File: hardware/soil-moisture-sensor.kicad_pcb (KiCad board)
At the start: 2 copper layers, 185.3 x 23 mm, 23 parts, among them J1 AVR ISP, J2 FTDI, SW1 SW_Push, U1 ATmega328P-AU, U2 NRF24L01_Breakout, U3 ATSHA204A, Y1 Resonator

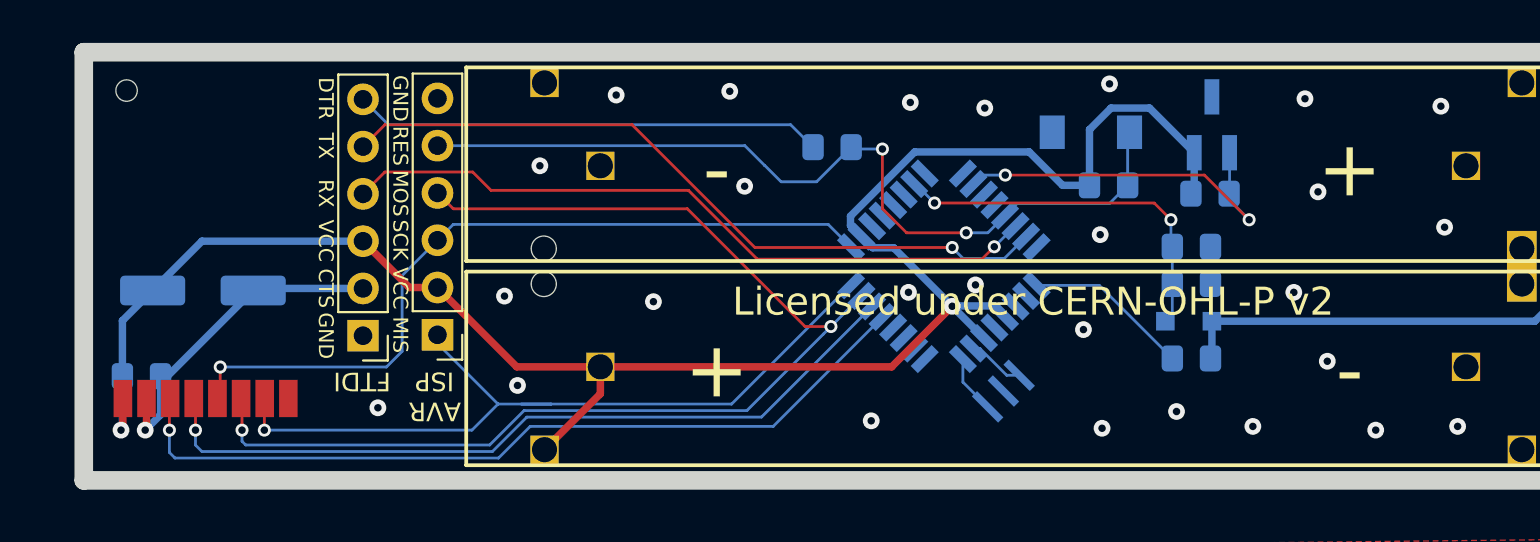
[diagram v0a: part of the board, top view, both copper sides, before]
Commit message: Add version number to silkscreen
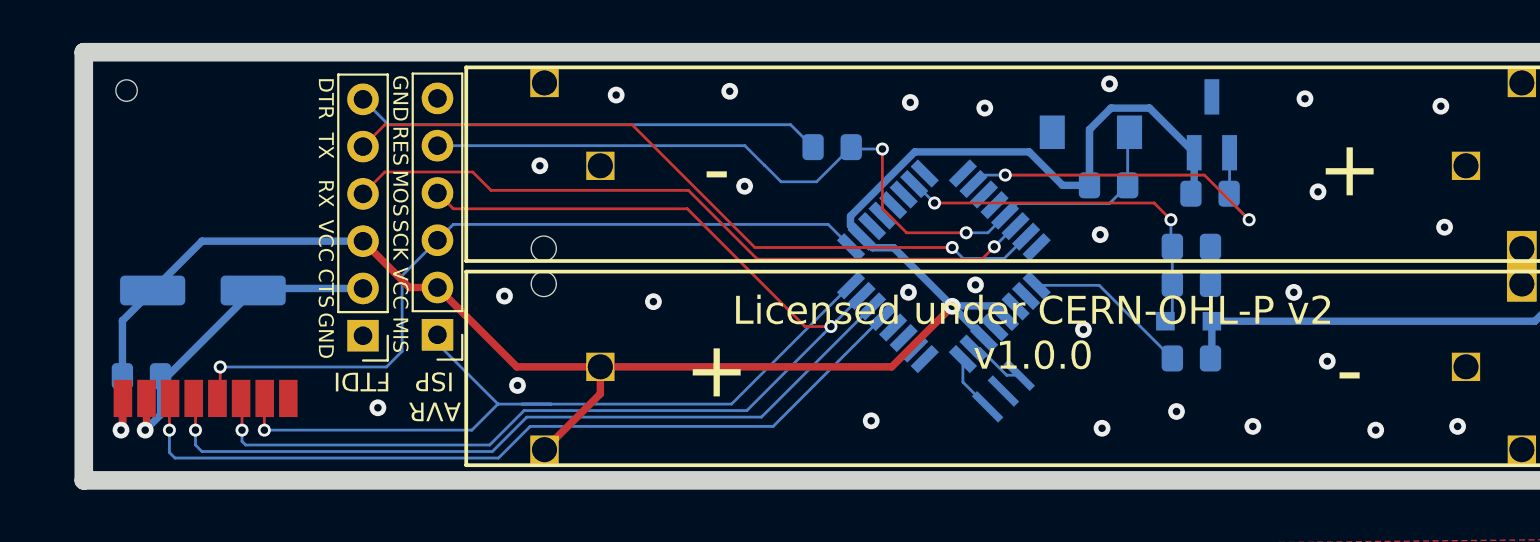
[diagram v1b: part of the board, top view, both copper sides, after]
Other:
- board text added: "Licensed under CERN-OHL-P v2 v1.0.0"
- board text removed: "Licensed under CERN-OHL-P v2"

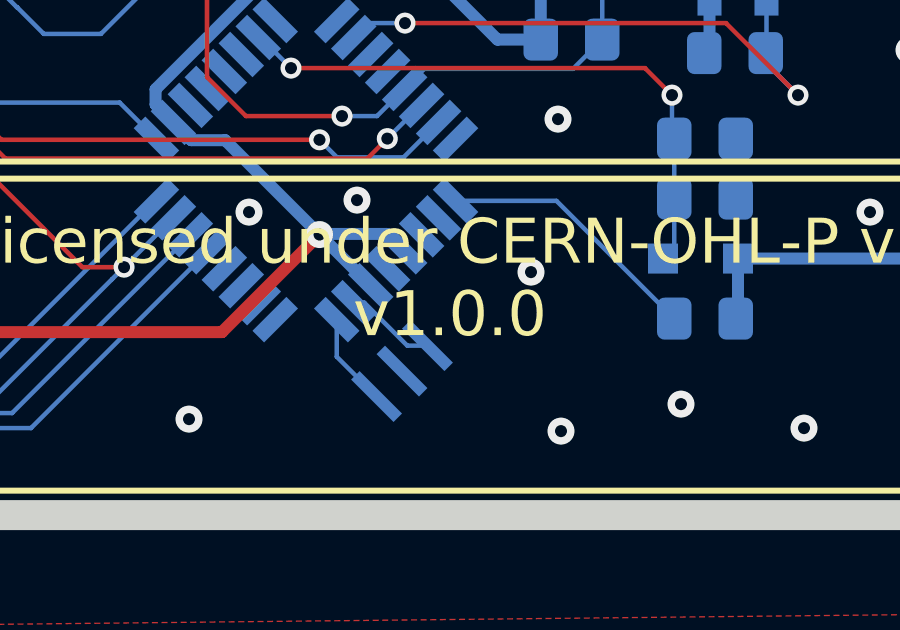
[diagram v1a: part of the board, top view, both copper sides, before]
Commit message: Restrict version to major.minor on the PCB
Also included the CERN-OHL-P v2 on the schematic.
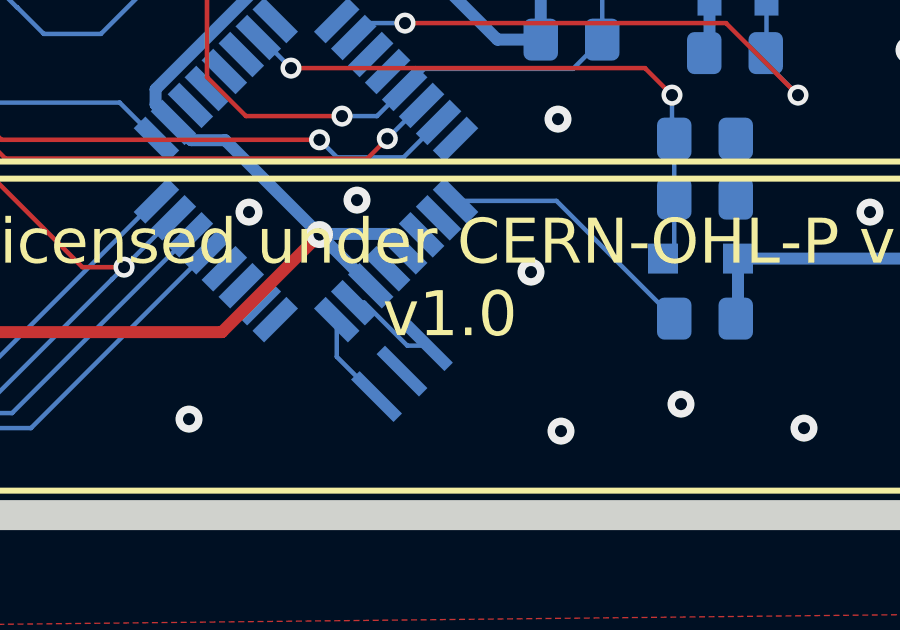
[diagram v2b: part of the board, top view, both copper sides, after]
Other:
- board text added: "Licensed under CERN-OHL-P v2 v1.0"
- board text removed: "Licensed under CERN-OHL-P v2 v1.0.0"

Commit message: Update footprint of NRF24L01-SMD
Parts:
- U2: footprint mysensors_radios:NRF24L01-SMD -> local_footprints:NRF24L01-SMD
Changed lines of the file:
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@@
     (add_net /Sensor_Track)
+  )
+  (module local_footprints:NRF24L01-SMD (layer F.Cu)
+    (at 71.8 112.6)
+    (fp_text reference U2 (at 0 1.1) (layer F.SilkS) hide
+      (effects (font (size 1 1) (thickness 0.15)))
+    )
+    (fp_text value NRF24L01_Breakout (at 0 2.8825) (layer F.Fab)
+      (effects (font (size 1 1) (thickness 0.15)))
+    )
+    (fp_line (start -6 -2.8) (end 6 -2.8) (layer F.CrtYd) (width 0.15))
+    (fp_line (start -6 8.7) (end -6 -9.3) (layer F.CrtYd) (width 0.15))
+    (fp_line (start 6 8.7) (end -6 8.7) (layer F.CrtYd) (width 0.15))
+    (fp_line (start 6 -9.3) (end 6 8.7) (layer F.CrtYd) (width 0.15))
+    (fp_line (start -6 -9.3) (end 6 -9.3) (layer F.CrtYd) (width 0.15))
+    (pad 8 smd rect (at 4.49 8.7) (size 1 2) (layers F.Cu F.Paste F.Mask)
+      (net 31 "Net-(U2-Pad8)"))
+    (pad 7 smd rect (at 3.22 8.7) (size 1 2) (layers F.Cu F.Paste F.Mask)
+      (net 3 MISO))
+    (pad 6 smd rect (at 1.95 8.7) (size 1 2) (layers F.Cu F.Paste F.Mask)
+      (net 5 MOSI))
+    (pad 5 smd rect (at 0.68 8.7) (size 1 2) (layers F.Cu F.Paste F.Mask)
+      (net 4 SCK))
+    (pad 4 smd rect (at -0.59 8.7) (size 1 2) (layers F.Cu F.Paste F.Mask)
+      (net 11 CSN))
+    (pad 3 smd rect (at -1.86 8.7) (size 1 2) (layers F.Cu F.Paste F.Mask)
+      (net 10 CE))
+    (pad 1 smd rect (at -3.13 8.7) (size 1 2) (layers F.Cu F.Paste F.Mask)
+      (net 1 GND))
+    (pad 2 smd rect (at -4.4 8.7) (size 1 2) (layers F.Cu F.Paste F.Mask)
+      (net 15 +BATT))
+    (model ${KIPRJMOD}/lib/mysensors.3dshapes/mysensors_radios.3dshapes/nrf24smd.wrl
+      (offset (xyz -146.3674978017807 73.65999889373779 0.7619999885559082))
+      (scale (xyz 0.395 0.395 0.395))
+      (rotate (xyz 0 0 0))
+    )
+    (model Housings_DFN_QFN.3dshapes/QFN-20-1EP_5x5mm_Pitch0.65mm.wrl
+      (offset (xyz 0.4190999937057495 -2.7685999584198 1.574799976348877))
+      (scale (xyz 1 1 1))
+      (rotate (xyz 0 0 0))
+    )
   )
   (module MyFootprints:BatteryHolder_Keystone_597_591_2AAA_3V locked (layer F.Cu)
@@
       (rotate (xyz 0 0 0))
     )
-  )
-  (module mysensors_radios:NRF24L01-SMD (layer F.Cu)
-    (at 71.8 112.6)
-    (fp_text reference U2 (at 0 1.1) (layer F.SilkS) hide
-      (effects (font (size 1 1) (thickness 0.15)))
-    )
-    (fp_text value NRF24L01_Breakout (at 0 2.8825) (layer F.Fab)
-      (effects (font (size 1 1) (thickness 0.15)))
-    )
-    (fp_line (start 5.5 -2.8) (end 6 -3.3) (layer Dwgs.User) (width 0.12))
-    (fp_line (start 6 -5.3) (end 3.5 -2.8) (layer Dwgs.User) (width 0.12))
-    (fp_line (start 1.5 -2.8) (end 6 -7.3) (layer Dwgs.User) (width 0.12))
-    (fp_line (start -0.5 -2.8) (end 6 -9.3) (layer Dwgs.User) (width 0.12))
-    (fp_line (start -2.5 -2.8) (end 4 -9.3) (layer Dwgs.User) (width 0.12))
-    (fp_line (start 2 -9.3) (end -4.5 -2.8) (layer Dwgs.User) (width 0.12))
-    (fp_line (start 0 -9.3) (end -6 -3.3) (layer Dwgs.User) (width 0.12))
-    (fp_line (start -6 -5.3) (end -2 -9.3) (layer Dwgs.User) (width 0.12))
-    (fp_line (start -4 -9.3) (end -6 -7.3) (layer Dwgs.User) (width 0.12))
-    (fp_line (start -6 -9.3) (end 6 -9.3) (layer F.CrtYd) (width 0.15))
-    (fp_line (start 6 -9.3) (end 6 8.7) (layer F.CrtYd) (width 0.15))
-    (fp_line (start 6 8.7) (end -6 8.7) (layer F.CrtYd) (width 0.15))
-    (fp_line (start -6 8.7) (end -6 -9.3) (layer F.CrtYd) (width 0.15))
-    (fp_line (start -6 -2.8) (end 6 -2.8) (layer F.CrtYd) (width 0.15))
-    (pad 8 smd rect (at 4.49 8.7) (size 1 2) (layers F.Cu F.Paste F.Mask)
-      (net 31 "Net-(U2-Pad8)"))
-    (pad 7 smd rect (at 3.22 8.7) (size 1 2) (layers F.Cu F.Paste F.Mask)
-      (net 3 MISO))
-    (pad 6 smd rect (at 1.95 8.7) (size 1 2) (layers F.Cu F.Paste F.Mask)
-      (net 5 MOSI))
-    (pad 5 smd rect (at 0.68 8.7) (size 1 2) (layers F.Cu F.Paste F.Mask)
-      (net 4 SCK))
-    (pad 4 smd rect (at -0.59 8.7) (size 1 2) (layers F.Cu F.Paste F.Mask)
-      (net 11 CSN))
-    (pad 3 smd rect (at -1.86 8.7) (size 1 2) (layers F.Cu F.Paste F.Mask)
-      (net 10 CE))
-    (pad 1 smd rect (at -3.13 8.7) (size 1 2) (layers F.Cu F.Paste F.Mask)
-      (net 1 GND))
-    (pad 2 smd rect (at -4.4 8.7) (size 1 2) (layers F.Cu F.Paste F.Mask)
-      (net 15 +BATT))
-    (model ${MYSLOCAL}/mysensors.3dshapes/mysensors_radios.3dshapes/nrf24smd.wrl
-      (offset (xyz -146.3674978017807 73.65999889373779 0.7619999885559082))
-      (scale (xyz 0.395 0.395 0.395))
-      (rotate (xyz 0 0 0))
-    )
